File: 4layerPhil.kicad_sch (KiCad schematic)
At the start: 52 parts, among them J1 USB_B_Micro, J2 Conn_01x05_Pin, J3 Conn_01x04_Pin, J5 Conn_01x05_Pin, J6 1140084168, SW1 SW_SPDT, SW2 BTN1, SW3 BTN2, SW4 BTN3, U1 AMS1117-3.3, U2 USBLC6-2P6, U3 STM32F103RCTx, Y1 16MHz

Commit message: completed all signal routes, switched btn placemenets
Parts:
- renumbered R4 to R3, R5 to R4, R3 to R5
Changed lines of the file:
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@@
 		(on_board yes)
 		(dnp no)
-		(property "Reference" "R4"
+		(property "Reference" "R3"
 			(at 231.902 79.248 90)
 			(effects
@@
 			(project "4layerPhil"
 				(path "/7ec3a92f-71da-4a6b-be29-ed63fa8d0fd2"
-					(reference "R4")
+					(reference "R3")
 					(unit 1)
 				)
@@
 		(on_board yes)
 		(dnp no)
-		(property "Reference" "R5"
+		(property "Reference" "R4"
 			(at 224.79 84.836 90)
 			(effects
@@
 			(project "4layerPhil"
 				(path "/7ec3a92f-71da-4a6b-be29-ed63fa8d0fd2"
-					(reference "R5")
+					(reference "R4")
 					(unit 1)
 				)
@@
 		(on_board yes)
 		(dnp no)
-		(property "Reference" "R3"
+		(property "Reference" "R5"
 			(at 138.43 66.04 90)
 			(effects
@@
 			(project "4layerPhil"
 				(path "/7ec3a92f-71da-4a6b-be29-ed63fa8d0fd2"
-					(reference "R3")
-					(unit 1)
-				)
+					(reference "R5")
+					(unit 1)
+				)

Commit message: Preparation for changing LDO to impulse regulator, SWDIO to a correct connector etc.
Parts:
- renumbered R18 to R16, R16 to R17, R19 to R18, R17 to R19
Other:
- note added: "MicroSD with card detect"
- moved on the sheet: C11, C12, C17, J6, R21, Y1

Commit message: Added gain
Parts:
- removed J1: USB_B_Micro, Connector_USB:USB_Micro-B_Wuerth_629105150521, symbol Connector:USB_B_Micro
- removed J5: Conn_01x05_Pin, Connector_PinHeader_2.54mm:PinHeader_1x05_P2.54mm_Vertical, symbol Connector:Conn_01x05_Pin
- added J1: USB_C_Receptacle_USB2.0_16P, symbol Connector:USB_C_Receptacle_USB2.0_16P
- added J5: Conn_01x06_Pin, Connector_PinHeader_2.54mm:PinHeader_1x06_P2.54mm_Vertical, symbol Connector:Conn_01x06_Pin
- added R22, R23: 100k, Resistor_SMD:R_0603_1608Metric, symbol Device:R
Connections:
- net +3V3: now also J5.1 (Pin_1), R22.2
- net D_USB+: now also J1.A6 (D+), J1.B6 (D+)
- net D_USB-: now also J1.A7 (D-), J1.B7 (D-)
- net GND: now also J1.A1 (GND), J1.A12 (GND), J1.B1 (GND), J1.B12 (GND), J5.6 (Pin_6), R23.2
- net I2S2_CK: now also J5.3 (Pin_3)
- net I2S2_SD: now also J5.4 (Pin_4)
- net I2S2_WS: now also J5.2 (Pin_2)
- net VBUS: now also J1.A4 (VBUS), J1.A9 (VBUS), J1.B4 (VBUS), J1.B9 (VBUS)
- new net I2S2_GAIN: J5.5 (Pin_5), R22.1, R23.1
- no-connect marks 33 -> 36
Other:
- note added: "MAX98357A full range of gain selection via 2 resistors"
- note removed: "USB App note AN4879"

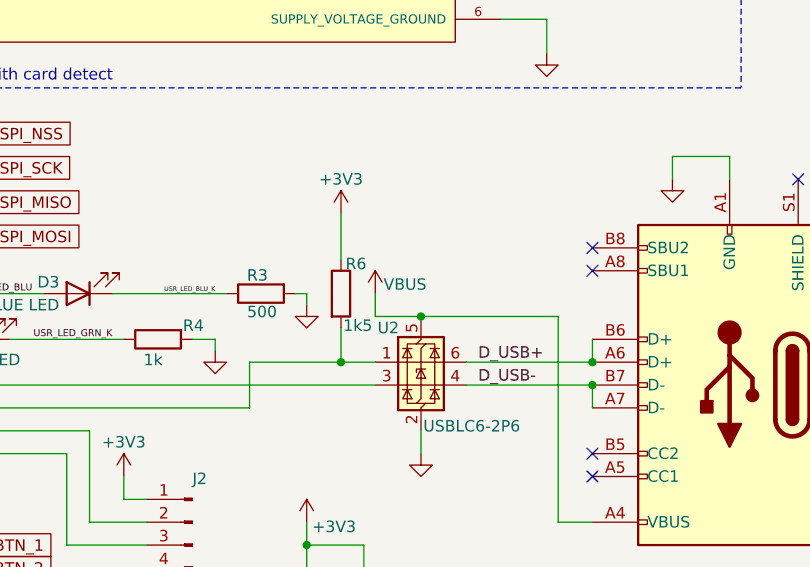
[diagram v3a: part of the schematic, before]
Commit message: assigned VBUS and GND as power lines for type-c receptacle schematic
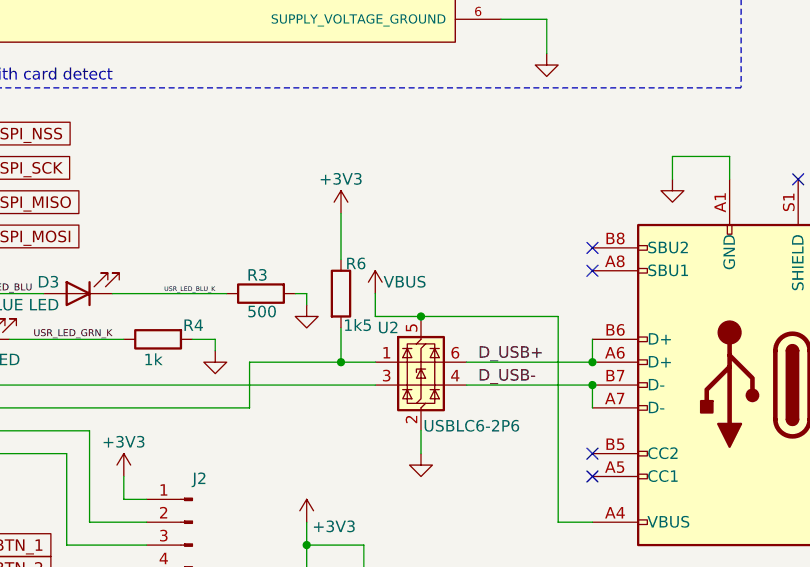
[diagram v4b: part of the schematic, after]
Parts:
- J1: footprint (none) -> Connector_USB:USB_C_Receptacle_GCT_USB4110
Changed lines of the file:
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@@
 		)
 		(property "Value" "VBUS"
-			(at 247.142 80.264 0)
+			(at 247.142 80.01 0)
 			(effects
 				(font
@@
 			)
 		)
-		(property "Footprint" ""
+		(property "Footprint" "Connector_USB:USB_C_Receptacle_GCT_USB4110"
 			(at 279.4 91.44 0)
 			(effects

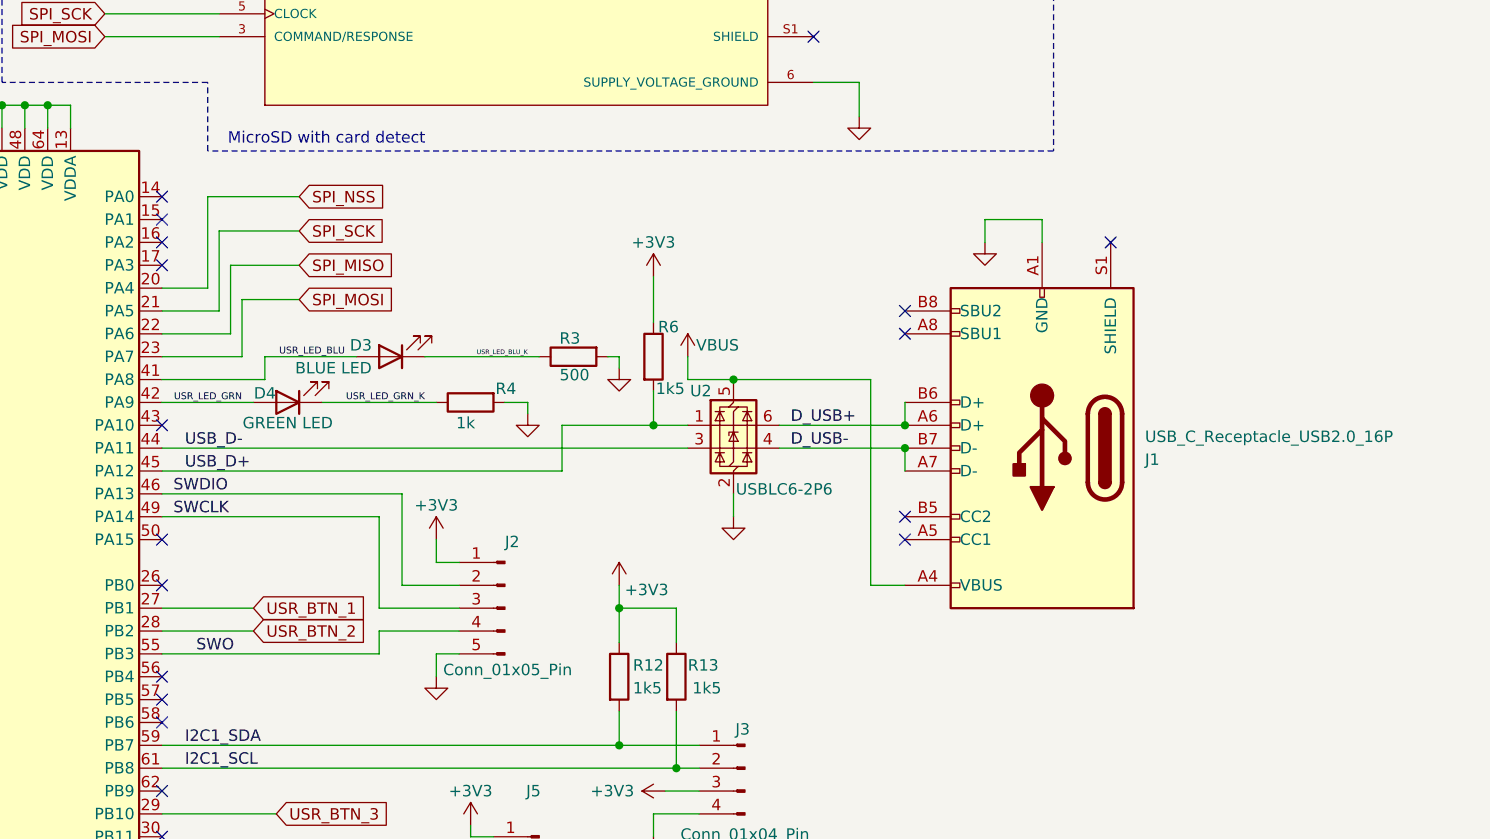
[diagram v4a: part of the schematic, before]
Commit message: Switched from MicroB to USB Type-C and smaller changes
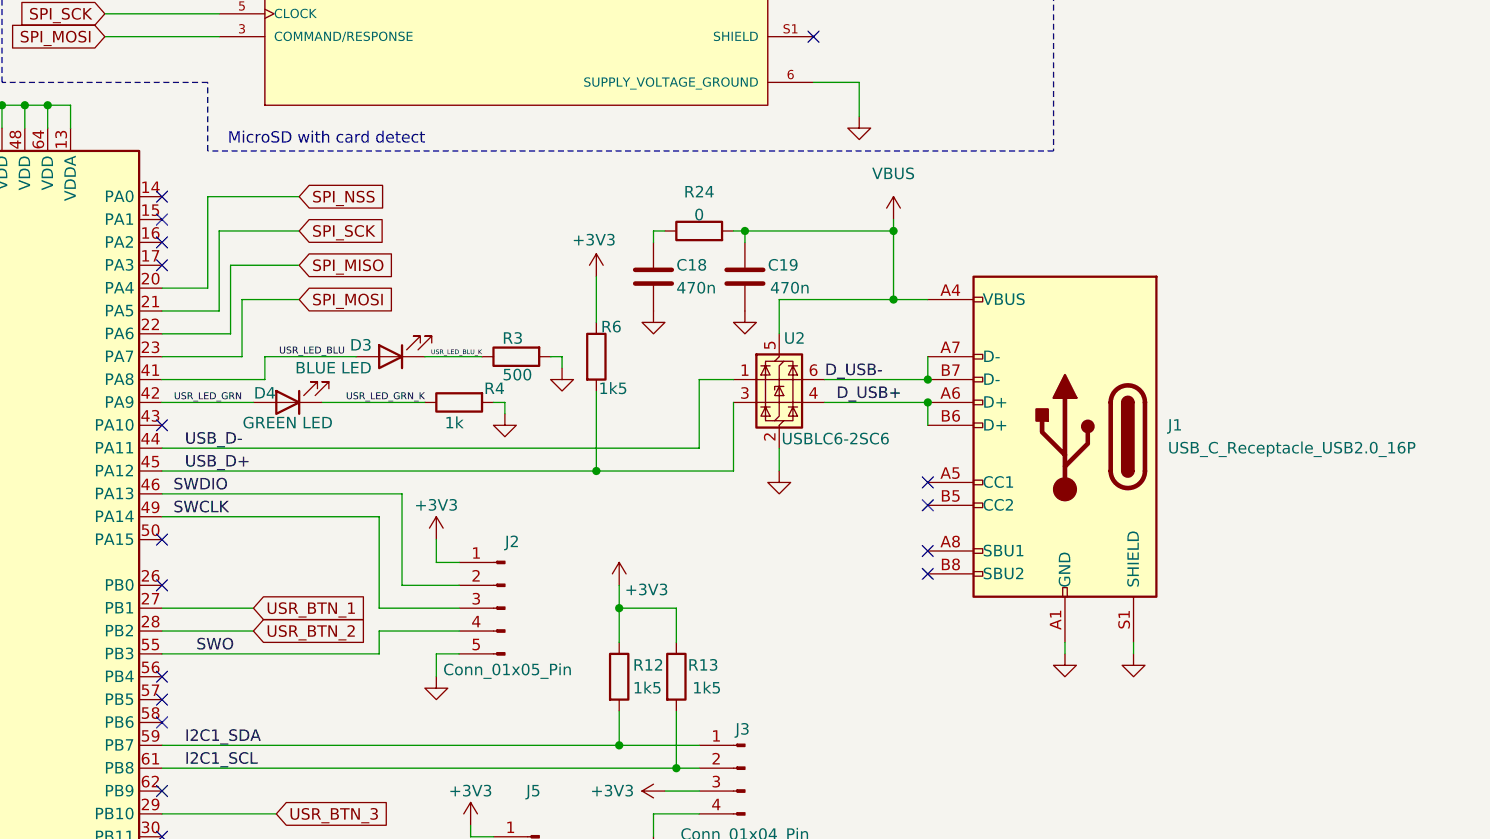
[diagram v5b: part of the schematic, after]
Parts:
- removed U2: USBLC6-2P6, Package_TO_SOT_SMD:SOT-666, symbol Power_Protection:USBLC6-2P6
- added C18, C19: 470n, symbol Device:C
- added R24: 0, symbol Device:R
- added U2: USBLC6-2SC6, Package_TO_SOT_SMD:SOT-23-6, symbol Power_Protection:USBLC6-2SC6
- J1: footprint Connector_USB:USB_C_Receptacle_GCT_USB4110 -> Connector_USB:USB_C_Receptacle_GCT_USB4105-xx-A_16P_TopMnt_Horizontal
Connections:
- net D_USB+: now also U2.4 (I/O2)
- net D_USB-: now also U2.6 (I/O1)
- net GND: now also J1.S1 (SHIELD), C18.2, C19.2, U2.2 (GND)
- net USB_D+: now also U2.3 (I/O2)
- net USB_D-: now also U2.1 (I/O1)
- net VBUS: now also C19.1, R24.2, U2.5 (VBUS)
- new net: C18.1, R24.1
- no-connect marks 36 -> 35
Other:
- moved on the sheet: J1, R3, R4, R6

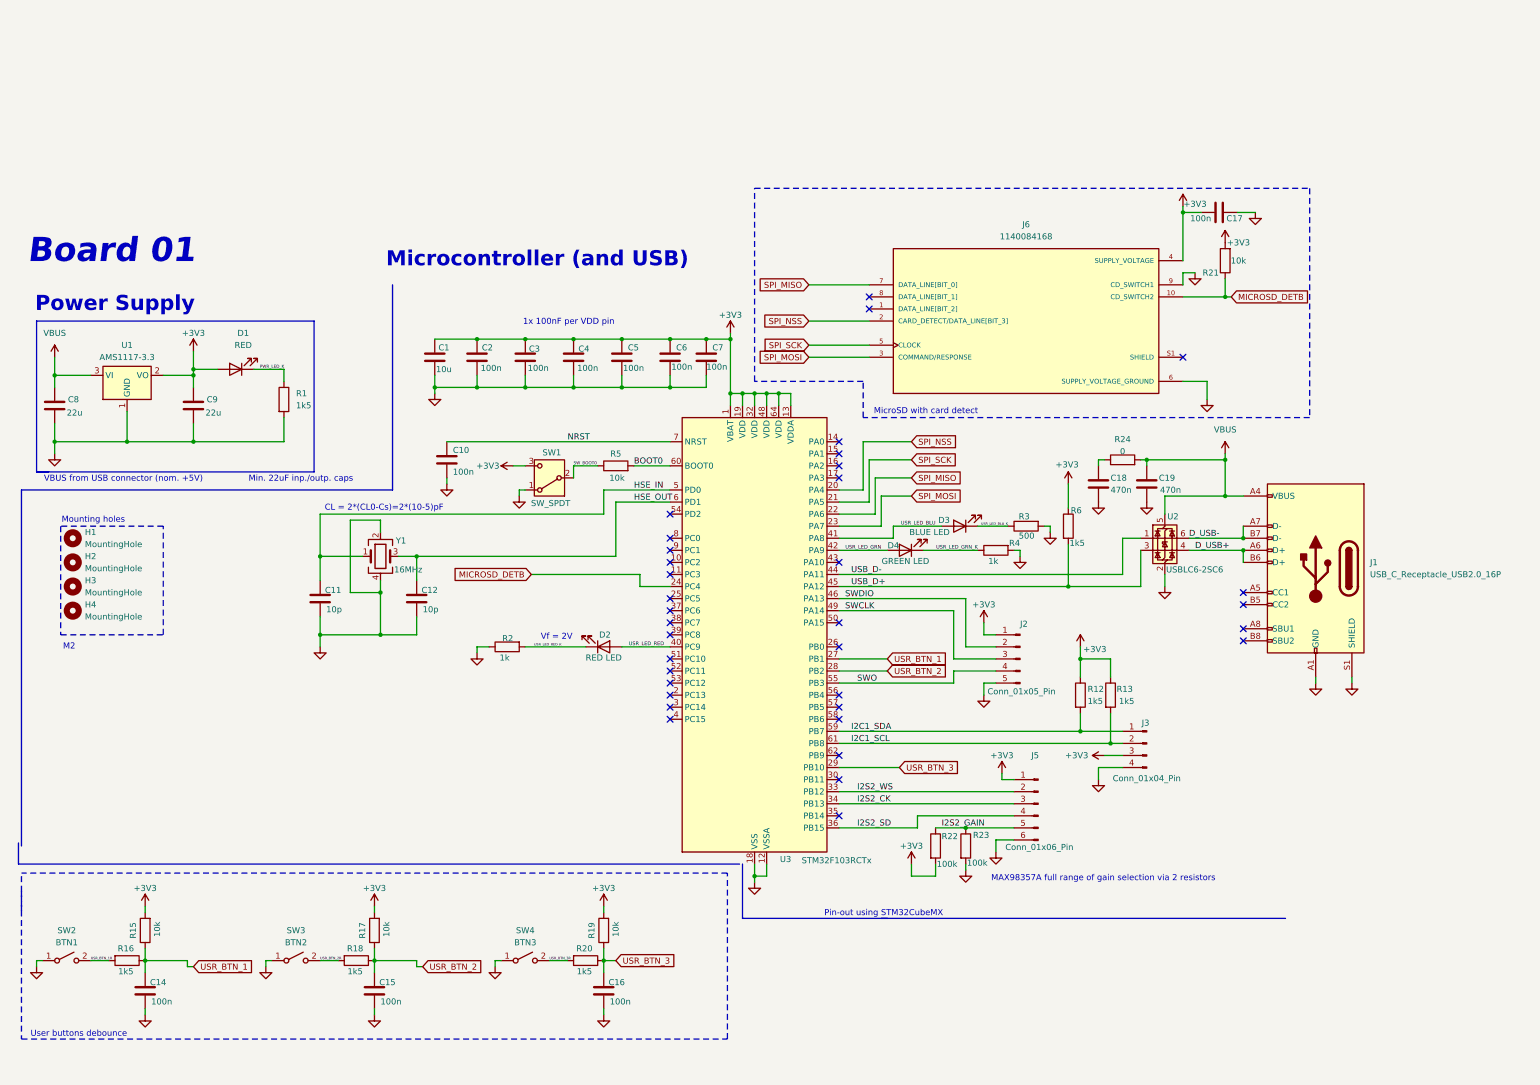
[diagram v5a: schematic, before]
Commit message: Created power supply circuit for new regulator, deleted ancient AMS1117
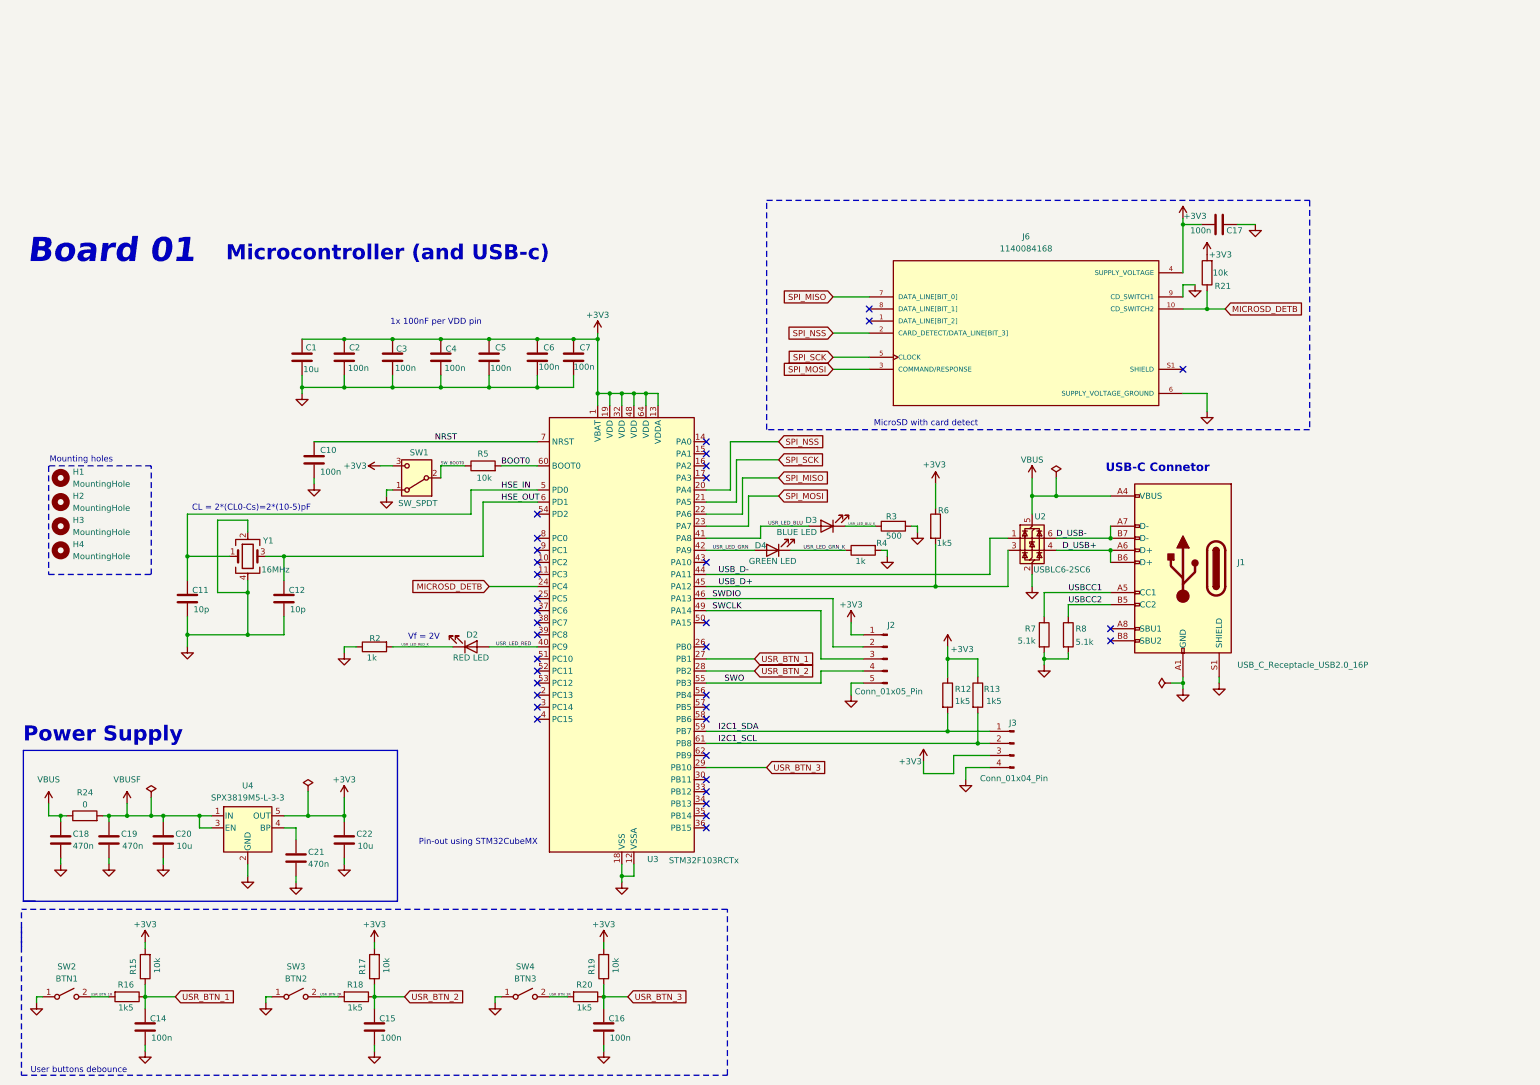
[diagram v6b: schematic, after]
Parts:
- removed C8, C9: 22u, Capacitor_SMD:C_0805_2012Metric, symbol Device:C
- removed D1: RED, LED_SMD:LED_0603_1608Metric, symbol Device:LED
- removed J5: Conn_01x06_Pin, Connector_PinHeader_2.54mm:PinHeader_1x06_P2.54mm_Vertical, symbol Connector:Conn_01x06_Pin
- removed R1: 1k5, Resistor_SMD:R_0603_1608Metric, symbol Device:R
- removed R22, R23: 100k, Resistor_SMD:R_0603_1608Metric, symbol Device:R
- removed U1: AMS1117-3.3, Package_TO_SOT_SMD:SOT-223-3_TabPin2, symbol Regulator_Linear:AMS1117-3.3
- added C20, C22: 10u, Capacitor_SMD:C_0603_1608Metric, symbol Device:C
- added C21: 470n, Capacitor_SMD:C_0603_1608Metric, symbol Device:C
- added R7, R8: 5.1k, Resistor_SMD:R_0603_1608Metric, symbol Device:R
- added U4: SPX3819M5-L-3-3, Package_TO_SOT_SMD:SOT-23-5, symbol Regulator_Linear:SPX3819M5-L-3-3
- C18, C19: footprint (none) -> Capacitor_SMD:C_0603_1608Metric
- R24: footprint (none) -> Resistor_SMD:R_0603_1608Metric
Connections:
- net +3V3: now also C22.1, U4.5 (OUT)
- net GND: now also C20.2, C21.2, C22.2, R7.2, R8.2, U4.2 (GND)
- net VBUS: now also C18.1, R24.1; no longer C19.1, R24.2
- net USBCC1: now reaches J1.A5 (CC1)
- net USBCC1: now also R7.1
- net USBCC2: now reaches J1.B5 (CC2)
- net USBCC2: now also R8.1
- net I2S2_CK: no longer names the net of U3.34 (PB13)
- net I2S2_SD: no longer names the net of U3.36 (PB15)
- net I2S2_WS: no longer names the net of U3.33 (PB12)
- new net: C21.1, U4.4 (BP)
- new net VBUSF: C19.1, C20.1, R24.2, U4.1 (IN), U4.3 (EN)
- no-connect marks 35 -> 36
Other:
- note added: "Microcontroller (and USB-c)"
- note added: "USB-C Connetor"
- note removed: "M2"
- note removed: "MAX98357A full range of gain selection via 2 resistors"
- note removed: "Microcontroller (and USB)"
- note removed: "Min. 22uF inp./outp. caps"
- note removed: "VBUS from USB connector (nom. +5V)"
- moved on the sheet: C1, C10, C11, C12, C14, C15, C16, C17, C18, C19, C2, C3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

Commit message: Added colours to schematic
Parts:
- removed H1, H2, H3, H4: MountingHole, MountingHole:MountingHole_2.2mm_M2, symbol Mechanical:MountingHole
- added FID1, FID2, FID3: Fiducial, Fiducial:Fiducial_1mm_Mask2mm, symbol Mechanical:Fiducial
- added MH1, MH2, MH3, MH4: M3, MountingHole:MountingHole_3.2mm_M3_Pad_Via, symbol Mechanical:MountingHole_Pad
- C1, C20, C22: footprint Capacitor_SMD:C_0603_1608Metric -> Capacitor_SMD:C_0805_2012Metric
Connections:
- net USR_LED_RED is gone; now on net LED_BLU: D2.2 (A), U3.40 (PC9)
- net GND: now also MH1.1, MH2.1, MH3.1, MH4.1
- net USB_D+: now also J1.A6 (D+), J1.B6 (D+), U2.6 (I/O1); no longer R6.2, U2.3 (I/O2), U3.45 (PA12)
- net USB_D-: now also J1.A7 (D-), J1.B7 (D-), U2.4 (I/O2); no longer U2.1 (I/O1), U3.44 (PA11)
- net BP_REG: now reaches C21.1, U4.4 (BP)
- removed net D_USB+: J1.A6 (D+), J1.B6 (D+), U2.4 (I/O2)
- removed net D_USB-: J1.A7 (D-), J1.B7 (D-), U2.6 (I/O1)
- net USR_LED_BLU renamed LED_BLU
- net USR_LED_BLU_K renamed LED_BLU_K
- net USR_LED_GRN renamed LED_GRN
- net USR_LED_GRN_K renamed LED_GRN_K
- net USR_LED_RED_K renamed LED_RED_K
- net VBUS renamed +VBUS
- net VBUSF renamed +VBUSF
- new net USB_D_ESD+: R6.2, U2.1 (I/O1), U3.45 (PA12)
- new net USB_D_ESD-: U2.3 (I/O2), U3.44 (PA11)
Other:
- moved on the sheet: U2
